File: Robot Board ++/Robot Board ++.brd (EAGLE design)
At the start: 68.6 x 76.2 mm, 123 parts, among them U10 74LVTH125.RGY, U11 SCHA4B0400, U12 BLUETOOTH-RN41", U13 XBEE-1XBEE-1_LOCK, U5 TPS5331[8/9].DQP, U6 TPS62082.DSG, U7 PCA9557.RGV, U8 MPU-6050

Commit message: Routing complete!
Lol, nap.
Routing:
- net 3.3V: track 363.3 -> 360.5 mm
- net GND: vias 182 -> 186
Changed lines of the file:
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@@
 <setting verticaltext="up"/>
 </settings>
-<grid distance="25" unitdist="mil" unit="mil" style="dots" multiple="2" display="yes" altdistance="5" altunitdist="mil" altunit="mil"/>
+<grid distance="0.25" unitdist="mm" unit="mm" style="dots" multiple="2" display="yes" altdistance="0.05" altunitdist="mm" altunit="mm"/>
 <layers>
 <layer number="1" name="Top" color="4" fill="1" visible="yes" active="yes"/>
@@
 <layer number="39" name="tKeepout" color="4" fill="11" visible="no" active="yes"/>
 <layer number="40" name="bKeepout" color="1" fill="11" visible="no" active="yes"/>
-<layer number="41" name="tRestrict" color="4" fill="10" visible="no" active="yes"/>
+<layer number="41" name="tRestrict" color="4" fill="10" visible="yes" active="yes"/>
 <layer number="42" name="bRestrict" color="1" fill="10" visible="no" active="yes"/>
 <layer number="43" name="vRestrict" color="2" fill="10" visible="no" active="yes"/>
@@
 <wire x1="31.365" y1="36.52" x2="31.365" y2="37.77" width="0.1524" layer="41"/>
 <wire x1="42.75" y1="26.75" x2="42.75" y2="28.5" width="0.1524" layer="41"/>
+<wire x1="24.5" y1="34" x2="25.75" y2="34" width="0.1524" layer="41"/>
 </plain>
 <attributes>
@@
 <wire x1="57.25" y1="0.75" x2="61.595" y2="5.095" width="0.3048" layer="1"/>
 <contactref element="R5" pad="1"/>
-<wire x1="34.036" y1="17.64" x2="33.25" y2="18.426" width="0.3048" layer="1"/>
-<wire x1="33.25" y1="18.426" x2="33.25" y2="22.75" width="0.3048" layer="1"/>
-<via x="33.25" y="22.75" extent="1-16" drill="0.3556"/>
-<wire x1="33.25" y1="22.75" x2="39.25" y2="22.75" width="0.3048" layer="16"/>
+<wire x1="34.036" y1="17.64" x2="33" y2="18.676" width="0.3048" layer="1"/>
+<wire x1="33" y1="18.676" x2="33" y2="22" width="0.3048" layer="1"/>
+<wire x1="33" y1="22" x2="33.75" y2="22.75" width="0.3048" layer="1"/>
+<via x="33.75" y="22.75" extent="1-16" drill="0.3556"/>
+<wire x1="33.75" y1="22.75" x2="39.25" y2="22.75" width="0.3048" layer="16"/>
 <wire x1="39.25" y1="22.75" x2="39.75" y2="22.25" width="0.3048" layer="16"/>
 <wire x1="39.75" y1="22.25" x2="45.75" y2="22.25" width="0.3048" layer="16"/>
@@
 <wire x1="4.445" y1="41.275" x2="4.445" y2="28.555" width="1.27" layer="1"/>
 <wire x1="4.445" y1="28.555" x2="4.5" y2="28.5" width="1.27" layer="1"/>
-<wire x1="33.25" y1="22.75" x2="29.5" y2="22.75" width="0.3048" layer="16"/>
+<wire x1="33.75" y1="22.75" x2="29.5" y2="22.75" width="0.3048" layer="16"/>
 <wire x1="29.5" y1="22.75" x2="28.75" y2="23.5" width="0.3048" layer="16"/>
 <wire x1="28.75" y1="23.5" x2="27" y2="23.5" width="0.3048" layer="16"/>
@@
 <wire x1="15.8275" y1="66.2275" x2="16.015" y2="66.04" width="0.254" layer="1"/>
 <wire x1="44.7022" y1="74.61" x2="42.61" y2="74.61" width="0.4064" layer="1"/>
-<wire x1="42.61" y1="74.61" x2="39.5" y2="71.5" width="0.4064" layer="1"/>
-<wire x1="39.5" y1="71.5" x2="34" y2="71.5" width="0.4064" layer="1"/>
-<via x="34" y="71.5" extent="1-16" drill="0.3556"/>
-<wire x1="34" y1="71.5" x2="34" y2="67.75" width="0.4064" layer="16"/>
-<wire x1="34" y1="67.75" x2="31.75" y2="65.5" width="0.4064" layer="16"/>
-<via x="31.75" y="65.5" extent="1-16" drill="0.3556"/>
-<wire x1="31.75" y1="65.5" x2="30.25" y2="64" width="0.4064" layer="1"/>
-<wire x1="30.25" y1="64" x2="30.25" y2="60.5" width="0.4064" layer="1"/>
+<wire x1="42.61" y1="74.61" x2="36.5" y2="68.5" width="0.4064" layer="1"/>
+<via x="36.5" y="68.5" extent="1-16" drill="0.3556"/>
+<wire x1="36.5" y1="68.5" x2="31.75" y2="63.75" width="0.4064" layer="16"/>
+<via x="31.75" y="63.75" extent="1-16" drill="0.3556"/>
+<wire x1="31.75" y1="63.75" x2="30.25" y2="62.25" width="0.4064" layer="1"/>
+<wire x1="30.25" y1="62.25" x2="30.25" y2="60.5" width="0.4064" layer="1"/>
 <wire x1="30.25" y1="60.5" x2="29.755" y2="60.005" width="0.4064" layer="1"/>
 <wire x1="29.755" y1="60.005" x2="28.96" y2="60.005" width="0.4064" layer="1"/>
@@
 <via x="39.37" y="31.75" extent="1-16" drill="0.3556"/>
 <via x="40.005" y="32.385" extent="1-16" drill="0.3556"/>
-<via x="38.735" y="32.385" extent="1-16" drill="0.3556"/>
-<via x="39.37" y="33.02" extent="1-16" drill="0.3556"/>
 <via x="40.64" y="33.02" extent="1-16" drill="0.3556"/>
 <via x="49.53" y="17.145" extent="1-16" drill="0.3556"/>
@@
 <wire x1="1.905" y1="21.59" x2="2.54" y2="22.225" width="0.3048" layer="1"/>
 <via x="38.5" y="50" extent="1-16" drill="0.3556"/>
+<via x="22.86" y="48.26" extent="1-16" drill="0.3556"/>
+<via x="40.005" y="28.575" extent="1-16" drill="0.3556"/>
+<via x="41.275" y="28.575" extent="1-16" drill="0.3556"/>
+<via x="41.275" y="29.845" extent="1-16" drill="0.3556"/>
+<via x="41.275" y="31.115" extent="1-16" drill="0.3556"/>
+<via x="41.275" y="32.385" extent="1-16" drill="0.3556"/>
 </signal>
 <signal name="SVRO0">
@@
 <wire x1="13.5" y1="60.5" x2="13.5" y2="61" width="0.3048" layer="16"/>
 <wire x1="13.5" y1="61" x2="14" y2="61.5" width="0.3048" layer="16"/>
-<wire x1="14" y1="61.5" x2="21.5" y2="61.5" width="0.3048" layer="16"/>
+<wire x1="14" y1="61.5" x2="21.25" y2="61.5" width="0.3048" layer="16"/>
 <wire x1="28.96" y1="67.205" x2="27.955" y2="67.205" width="0.3048" layer="1"/>
 <wire x1="27.955" y1="67.205" x2="27.75" y2="67" width="0.3048" layer="1"/>
 <wire x1="27.75" y1="67" x2="27.75" y2="65.75" width="0.3048" layer="1"/>
 <wire x1="27.75" y1="65.75" x2="27" y2="65" width="0.3048" layer="1"/>
-<wire x1="27" y1="65" x2="25" y2="65" width="0.3048" layer="1"/>
-<wire x1="25" y1="65" x2="24.75" y2="64.75" width="0.3048" layer="1"/>
-<wire x1="21.5" y1="61.5" x2="24.75" y2="64.75" width="0.3048" layer="16"/>
-<via x="24.75" y="64.75" extent="1-16" drill="0.3556"/>
+<wire x1="27" y1="65" x2="24.75" y2="65" width="0.3048" layer="1"/>
+<wire x1="24.75" y1="65" x2="24.5" y2="64.75" width="0.3048" layer="1"/>
+<wire x1="21.25" y1="61.5" x2="24.5" y2="64.75" width="0.3048" layer="16"/>
+<via x="24.5" y="64.75" extent="1-16" drill="0.3556"/>
 </signal>
 <signal name="BT.RXI">
@@
 <wire x1="6.985" y1="15.875" x2="5.715" y2="14.605" width="0.3048" layer="1"/>
 <wire x1="5.715" y1="12.065" x2="6.985" y2="10.795" width="0.3048" layer="1"/>
-<wire x1="66.675" y1="15.875" x2="67.945" y2="14.605" width="0.3048" layer="16"/>
-<wire x1="67.945" y1="14.605" x2="67.945" y2="12.065" width="0.3048" layer="16"/>
-<wire x1="67.945" y1="12.065" x2="66.675" y2="10.795" width="0.3048" layer="16"/>
 <wire x1="11.43" y1="27.94" x2="11.43" y2="27.305" width="0.3048" layer="16"/>
 <wire x1="11.43" y1="27.305" x2="6.985" y2="22.86" width="0.3048" layer="16"/>
@@
 <wire x1="65.405" y1="14.605" x2="60.96" y2="14.605" width="0.3048" layer="1"/>
 <wire x1="60.96" y1="14.605" x2="59.5" y2="13.145" width="0.3048" layer="1"/>
-<wire x1="66.675" y1="15.875" x2="67.945" y2="17.145" width="0.3048" layer="16"/>
-<wire x1="67.945" y1="17.145" x2="67.945" y2="44.555" width="0.3048" layer="16"/>
 <wire x1="58.7025" y1="71.805" x2="58.7025" y2="71.0475" width="0.3048" layer="1"/>
 <wire x1="58.7025" y1="71.0475" x2="59.5" y2="70.25" width="0.3048" layer="1"/>
@@
 <wire x1="66.25" y1="45.75" x2="62.5" y2="49.5" width="0.3048" layer="1"/>
 <wire x1="62.5" y1="49.5" x2="62.5" y2="50.75" width="0.3048" layer="1"/>
-<wire x1="67.945" y1="44.555" x2="66.75" y2="45.75" width="0.3048" layer="16"/>
-<wire x1="66.75" y1="45.75" x2="66.25" y2="45.75" width="0.3048" layer="16"/>
 <via x="62.5" y="50.75" extent="1-16" drill="0.3556"/>
 <wire x1="62.5" y1="50.75" x2="62.5" y2="52.75" width="0.3048" layer="16"/>
 <via x="62.5" y="52.75" extent="1-16" drill="0.3556"/>
 <wire x1="62.5" y1="52.75" x2="64.25" y2="54.5" width="0.3048" layer="1"/>
+<wire x1="66.675" y1="15.875" x2="68" y2="14.55" width="0.3048" layer="16"/>
+<wire x1="68" y1="14.55" x2="68" y2="12.12" width="0.3048" layer="16"/>
+<wire x1="68" y1="12.12" x2="66.675" y2="10.795" width="0.3048" layer="16"/>
+<wire x1="66.675" y1="15.875" x2="68" y2="17.2" width="0.3048" layer="16"/>
+<wire x1="68" y1="17.2" x2="68" y2="44.5" width="0.3048" layer="16"/>
+<wire x1="68" y1="44.5" x2="66.75" y2="45.75" width="0.3048" layer="16"/>
+<wire x1="66.75" y1="45.75" x2="66.25" y2="45.75" width="0.3048" layer="16"/>
 </signal>
 <signal name="I2C.SDA">
@@
 <via x="14.605" y="31.75" extent="1-16" drill="0.3556"/>
 <wire x1="14.605" y1="31.75" x2="13.335" y2="31.75" width="0.3048" layer="16"/>
-<wire x1="66.675" y1="8.255" x2="67.945" y2="9.525" width="0.3048" layer="1"/>
-<wire x1="67.945" y1="9.525" x2="67.945" y2="23.555" width="0.3048" layer="1"/>
 <wire x1="61.595" y1="28.575" x2="60.325" y2="29.845" width="0.3048" layer="16"/>
 <wire x1="60.325" y1="29.845" x2="58.42" y2="29.845" width="0.3048" layer="16"/>
@@
 <wire x1="62" y1="28.17" x2="61.595" y2="28.575" width="0.3048" layer="1"/>
 <wire x1="62" y1="25.25" x2="66.25" y2="25.25" width="0.3048" layer="16"/>
-<wire x1="67.945" y1="23.555" x2="66.25" y2="25.25" width="0.3048" layer="1"/>
 <via x="66.25" y="25.25" extent="1-16" drill="0.3556"/>
 <wire x1="44" y1="26" x2="50.5" y2="26" width="0.3048" layer="1"/>
 <wire x1="50.5" y1="26" x2="53.71" y2="29.21" width="0.3048" layer="1"/>
 <wire x1="53.71" y1="29.21" x2="53.975" y2="29.21" width="0.3048" layer="1"/>
+<wire x1="66.675" y1="8.255" x2="68" y2="9.58" width="0.3048" layer="1"/>
+<wire x1="68" y1="9.58" x2="68" y2="23.5" width="0.3048" layer="1"/>
+<wire x1="68" y1="23.5" x2="66.25" y2="25.25" width="0.3048" layer="1"/>
 </signal>
 <signal name="N$9">
@@
 </signal>
 </signals>
+<errors>
+</errors>
 </board>
 </drawing>

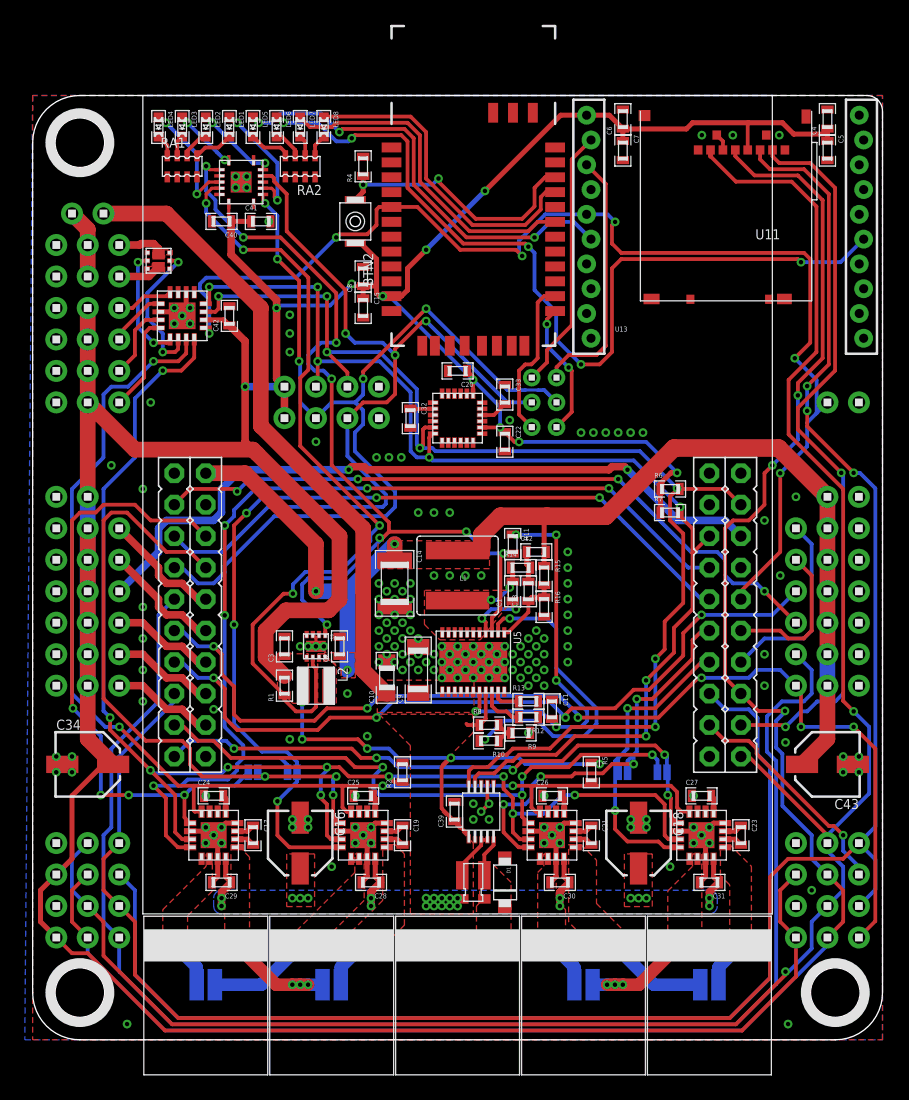
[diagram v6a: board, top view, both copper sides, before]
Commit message: Removed SMD jumpers for Motors. Will put onto adapter instead. Layout and silkscreen on board tenatively completed. Schematic will be cleaned up after Senior design paper due tomorrow.
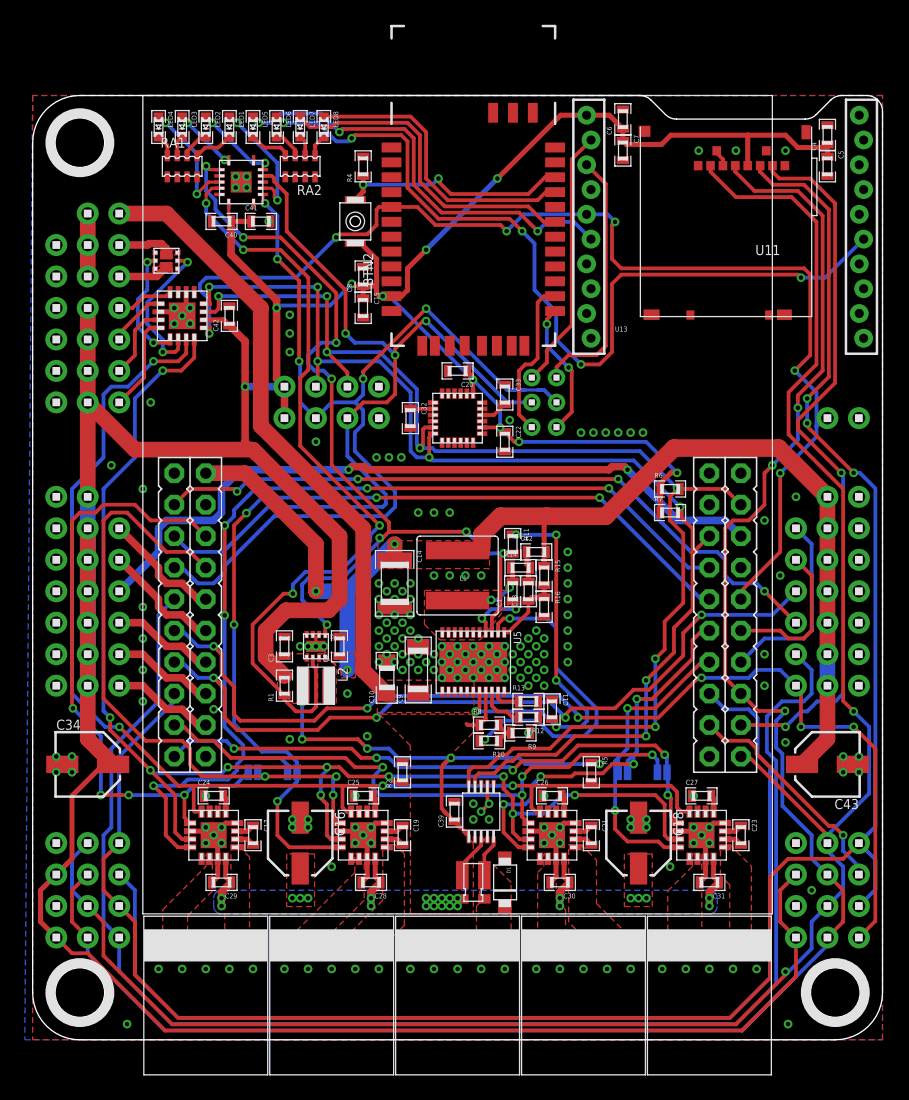
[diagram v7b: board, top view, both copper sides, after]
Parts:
- removed J1, J2, J3, J4: (no value), solderjumper:2.XL
- moved U11 1.27 mm to (62.9, 73.7)
- moved H24 1.27 mm to (64.1, 50.2)
- moved H27 1.27 mm to (4.45, 66.7)
- moved C4 1.27 mm to (64.1, 73.0)
- moved C5 1.27 mm to (64.1, 70.5)
- moved U$55 0.63 mm to (10.8, 62.9)
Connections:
- net M0+: no longer J1.1
- net M0-: no longer J2.1
- net M1+: no longer J1.2
- net M1-: no longer J2.2
- net M2+: no longer J3.1
- net M2-: no longer J4.1
- net M3+: no longer J3.2
- net M3-: no longer J4.2
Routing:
- net M0-: track 9.51 -> 0.00 mm, vias 3 -> 0
- net M3+: track 9.51 -> 0.00 mm, vias 3 -> 0
- net M1+: track 8.24 -> 0.00 mm
- net M2-: track 8.24 -> 0.00 mm
- net M3-: track 3.91 -> 0.00 mm
- net M2+: track 3.91 -> 0.00 mm
- net M1-: track 3.91 -> 0.00 mm
- net M0+: track 3.91 -> 0.00 mm
- net !RST: track 96.9 -> 94.0 mm
- net BT.RESET: track 21.6 -> 19.1 mm
- net BT.CONNECT: track 26.2 -> 24.0 mm
- net SPI.MOSI: track 166.5 -> 165.0 mm
- net VBAT: track 76.8 -> 75.5 mm
- net SPI.FSS: track 59.6 -> 58.3 mm
- net SPI.SCLK: track 152.0 -> 150.7 mm
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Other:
- outline, holes or cut-outs redrawn
- board text added: "+"
- board text added: "-"
- board text added: "0"
- board text added: "1"
- board text added: "1 || 2"
- board text added: "2"
- board text added: "3"
- board text added: "3.3v"
- board text added: "4"
- board text added: "5"
- board text added: "5v"
- board text added: "AnomalousMaker.com"
- board text added: "Associate"
- board text added: "Bluetooth"
- board text added: "CS"
- board text added: "Connect"
- board text added: "Cruz Monrreal II"
- board text added: "ENC 0|2"
- board text added: "ENC 1|3"
- board text added: "Factory RST"
- board text added: "GND"
- board text added: "I2C"
- board text added: "M0"
- board text added: "M1"
- board text added: "M2"
- board text added: "M3"
- board text added: "MISO"
- board text added: "MOSI"
- board text added: "RSSI"
- board text added: "RST"
- board text added: "Robotics Booster Pack"
- board text added: "RxI"
- board text added: "SCL"
- board text added: "SCLK"
- board text added: "SDA"
- board text added: "Status"
- board text added: "TxO"
- board text added: "UART"
- board text added: "VBAT"
- board text added: "VIN"
- board text added: "XBee"
- board text added: "~"
- board text removed: "ENC[0/1]"
- board text removed: "ENC[2/3]"
